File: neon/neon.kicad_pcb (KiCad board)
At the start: 2 copper layers, 60 x 50 mm, 45 parts, among them J2 V3V3-GND, J3 V3V3-GND, J4 V3V3-GND, J5 V3V3-VIO, Q1 BC807, Q2 BC807, Q3 BC807, Q4 BC807, Q5 BC807, Q6 BC807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

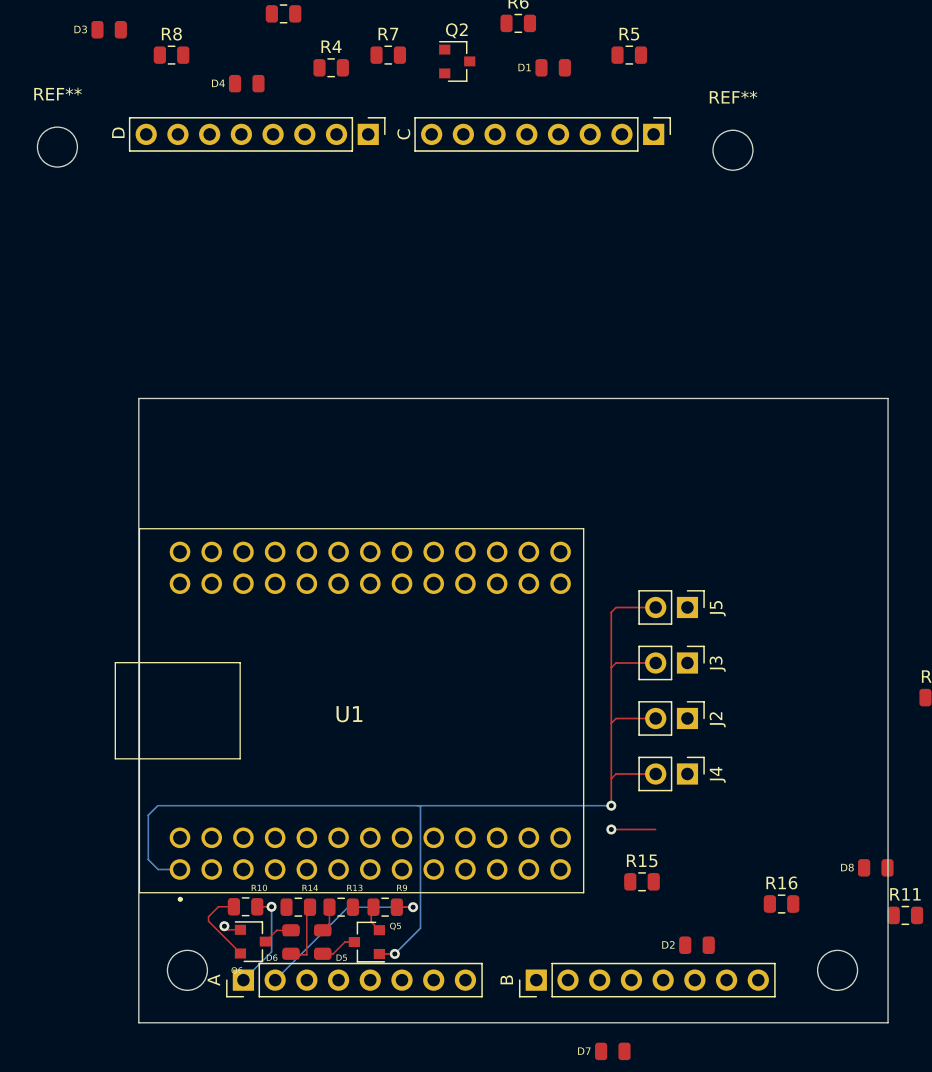
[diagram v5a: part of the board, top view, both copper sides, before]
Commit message: Labels adjustments
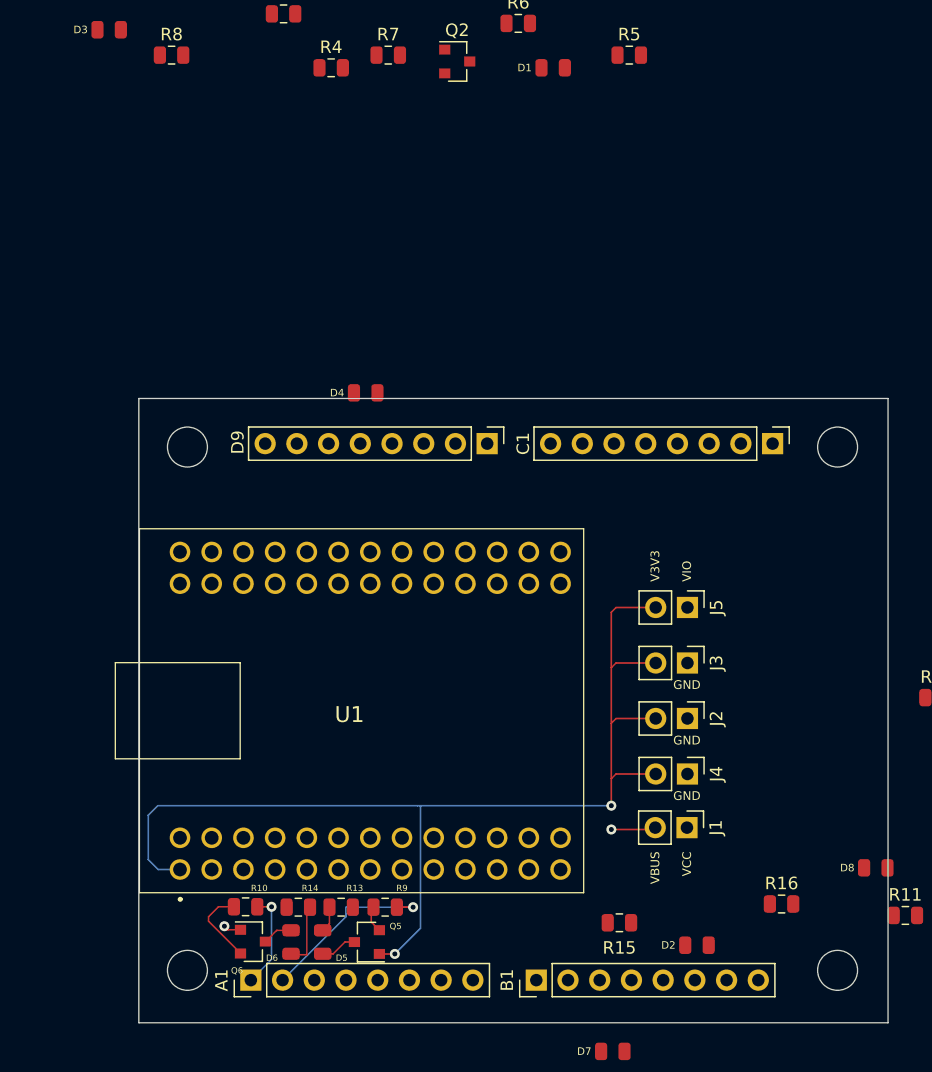
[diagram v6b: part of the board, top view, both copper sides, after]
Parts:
- removed the REF** at (163.1, 60.0)
- removed the REF** at (109.0, 59.8)
- added J1: VBUS-VCC, Connector_PinHeader_2.54mm:PinHeader_1x02_P2.54mm_Vertical, F.Cu at (159.4, 114.3)
- added REF**: MountingHole_3.2mm_M3, MountingHole:MountingHole_3.2mm_M3, F.Cu at (171.4, 83.8)
- added REF**: MountingHole_3.2mm_M3, MountingHole:MountingHole_3.2mm_M3, F.Cu at (119.4, 83.8)
- moved C1 26.5 mm to (166.2, 83.5)
- moved D4 26.5 mm to (133.7, 79.5)
- moved D9 26.5 mm to (143.4, 83.5)
- moved R15 3.75 mm to (154.0, 121.9)
- moved A1 0.60 mm to (124.5, 126.5)
- renumbered A to A1, B to B1, C to C1, D to D9
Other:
- board text added: "GND"
- board text added: "V3V3"
- board text added: "VBUS"
- board text added: "VCC"
- board text added: "VIO"
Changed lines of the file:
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@@
   (general
     (thickness 1.6)
-    (drawings 8)
-    (tracks 68)
+    (drawings 15)
+    (tracks 69)
     (zones 0)
-    (modules 45)
+    (modules 46)
     (nets 77)
   )
@@
     (add_net V3V3)
   )
+  (module Connector_PinHeader_2.54mm:PinHeader_1x02_P2.54mm_Vertical (layer F.Cu)
+    (at 159.385 114.3 270)
+    (descr "Through hole straight pin header, 1x02, 2.54mm pitch, single row")
+    (tags "Through hole pin header THT 1x02 2.54mm single row")
+    (fp_text reference J1 (at 0 -2.33 90) (layer F.SilkS)
+      (effects (font (size 1 1) (thickness 0.15)))
+    )
+    (fp_text value VBUS-VCC (at 0 4.87 90) (layer F.Fab)
+      (effects (font (size 1 1) (thickness 0.15)))
+    )
+    (fp_text user %R (at 0 1.27) (layer F.Fab)
+      (effects (font (size 1 1) (thickness 0.15)))
+    )
+    (fp_line (start -0.635 -1.27) (end 1.27 -1.27) (layer F.Fab) (width 0.1))
+    (fp_line (start 1.27 -1.27) (end 1.27 3.81) (layer F.Fab) (width 0.1))
+    (fp_line (start 1.27 3.81) (end -1.27 3.81) (layer F.Fab) (width 0.1))
+    (fp_line (start -1.27 3.81) (end -1.27 -0.635) (layer F.Fab) (width 0.1))
+    (fp_line (start -1.27 -0.635) (end -0.635 -1.27) (layer F.Fab) (width 0.1))
+    (fp_line (start -1.33 3.87) (end 1.33 3.87) (layer F.SilkS) (width 0.12))
+    (fp_line (start -1.33 1.27) (end -1.33 3.87) (layer F.SilkS) (width 0.12))
+    (fp_line (start 1.33 1.27) (end 1.33 3.87) (layer F.SilkS) (width 0.12))
+    (fp_line (start -1.33 1.27) (end 1.33 1.27) (layer F.SilkS) (width 0.12))
+    (fp_line (start -1.33 0) (end -1.33 -1.33) (layer F.SilkS) (width 0.12))
+    (fp_line (start -1.33 -1.33) (end 0 -1.33) (layer F.SilkS) (width 0.12))
+    (fp_line (start -1.8 -1.8) (end -1.8 4.35) (layer F.CrtYd) (width 0.05))
+    (fp_line (start -1.8 4.35) (end 1.8 4.35) (layer F.CrtYd) (width 0.05))
+    (fp_line (start 1.8 4.35) (end 1.8 -1.8) (layer F.CrtYd) (width 0.05))
+    (fp_line (start 1.8 -1.8) (end -1.8 -1.8) (layer F.CrtYd) (width 0.05))
+    (pad 2 thru_hole oval (at 0 2.54 270) (size 1.7 1.7) (drill 1) (layers *.Cu *.Mask)
+      (net 17 /FT4232H.sch/VBUS))
+    (pad 1 thru_hole rect (at 0 0 270) (size 1.7 1.7) (drill 1) (layers *.Cu *.Mask)
+      (net 50 /FT4232H.sch/VCC))
+    (model ${KISYS3DMOD}/Connector_PinHeader_2.54mm.3dshapes/PinHeader_1x02_P2.54mm_Vertical.wrl
+      (at (xyz 0 0 0))
+      (scale (xyz 1 1 1))
+      (rotate (xyz 0 0 0))
+    )
+  )
   (module Connector_PinHeader_2.54mm:PinHeader_1x08_P2.54mm_Vertical (layer F.Cu)
-    (at 123.8644 126.5136 90)
+    (at 124.46 126.5136 90)
     (descr "Through hole straight pin header, 1x08, 2.54mm pitch, single row")
     (tags "Through hole pin header THT 1x08 2.54mm single row")
-    (fp_text reference A (at 0 -2.33 90) (layer F.SilkS)
+    (fp_text reference A1 (at 0 -2.33 90) (layer F.SilkS)
       (effects (font (size 1 1) (thickness 0.15)))
     )
@@
   )
   (module neon_footprints:LED_0805_2012Metric (layer F.Cu)
-    (at 124.1295 54.716)
+    (at 133.6545 79.481)
     (descr "LED SMD 0805 (2012 Metric), square (rectangular) end terminal, IPC_7351 nominal, (Body size source: https://docs.google.com/spreadsheets/d/1BsfQQcO9C6DZCsRaXUlFlo91Tg2WpOkGARC1WS5S8t0/edit?usp=sharing), generated with kicad-footprint-generator")
     (tags diode)
@@
   )
   (module MountingHole:MountingHole_3.2mm_M3 (layer F.Cu)
-    (at 163.07 60.05)
+    (at 171.45 83.82)
     (descr "Mounting Hole 3.2mm, no annular, M3")
     (tags "mounting hole 3.2mm no annular m3")
     (attr virtual)
-    (fp_text reference REF** (at 0 -4.2) (layer F.SilkS)
+    (fp_text reference REF** (at 1.905 4.445) (layer F.SilkS) hide
       (effects (font (size 1 1) (thickness 0.15)))
     )
@@
   )
   (module MountingHole:MountingHole_3.2mm_M3 (layer F.Cu)
-    (at 108.968 59.796)
+    (at 119.38 83.82)
     (descr "Mounting Hole 3.2mm, no annular, M3")
     (tags "mounting hole 3.2mm no annular m3")
     (attr virtual)
-    (fp_text reference REF** (at 0 -4.2) (layer F.SilkS)
+    (fp_text reference REF** (at -1.27 4.445) (layer F.SilkS) hide
       (effects (font (size 1 1) (thickness 0.15)))
     )
@@
   )
   (module Resistor_SMD:R_0805_2012Metric (layer F.Cu)
-    (at 155.7899 118.6396)
+    (at 153.9725 121.92)
     (descr "Resistor SMD 0805 (2012 Metric), square (rectangular) end terminal, IPC_7351 nominal, (Body size source: https://docs.google.com/spreadsheets/d/1BsfQQcO9C6DZCsRaXUlFlo91Tg2WpOkGARC1WS5S8t0/edit?usp=sharing), generated with kicad-footprint-generator")
     (tags resistor)
     (attr smd)
-    (fp_text reference R15 (at 0 -1.65) (layer F.SilkS)
+    (fp_text reference R15 (at 0 2.0104) (layer F.SilkS)
       (effects (font (size 1 1) (thickness 0.15)))
     )
@@
   )
   (module Connector_PinHeader_2.54mm:PinHeader_1x08_P2.54mm_Vertical (layer F.Cu)
-    (at 156.72 58.78 270)
+    (at 166.245 83.545 270)
     (descr "Through hole straight pin header, 1x08, 2.54mm pitch, single row")
     (tags "Through hole pin header THT 1x08 2.54mm single row")
-    (fp_text reference C (at 0 19.974 90) (layer F.SilkS)
+    (fp_text reference C1 (at 0 19.974 90) (layer F.SilkS)
       (effects (font (size 1 1) (thickness 0.15)))
     )
@@
   )
   (module Connector_PinHeader_2.54mm:PinHeader_1x08_P2.54mm_Vertical (layer F.Cu)
-    (at 133.86 58.78 270)
+    (at 143.385 83.545 270)
     (descr "Through hole straight pin header, 1x08, 2.54mm pitch, single row")
     (tags "Through hole pin header THT 1x08 2.54mm single row")
-    (fp_text reference D (at -0.106 19.974 90) (layer F.SilkS)
+    (fp_text reference D9 (at -0.106 19.974 90) (layer F.SilkS)
       (effects (font (size 1 1) (thickness 0.15)))
     )
@@
     (descr "Through hole straight pin header, 1x08, 2.54mm pitch, single row")
     (tags "Through hole pin header THT 1x08 2.54mm single row")
-    (fp_text reference B (at 0 -2.33 90) (layer F.SilkS)
+    (fp_text reference B1 (at 0 -2.33 90) (layer F.SilkS)
       (effects (font (size 1 1) (thickness 0.15)))
     )
@@
       (rotate (xyz 0 0 0))
     )
+  )
+  (gr_text GND (at 159.385 111.76) (layer F.SilkS)
+    (effects (font (size 0.7 0.7) (thickness 0.175)))
+  )
+  (gr_text GND (at 159.385 107.315) (layer F.SilkS)
+    (effects (font (size 0.7 0.7) (thickness 0.175)))
+  )
+  (gr_text GND (at 159.385 102.87) (layer F.SilkS)
+    (effects (font (size 0.7 0.7) (thickness 0.175)))
+  )
+  (gr_text V3V3 (at 156.845 94.615 90) (layer F.SilkS)
+    (effects (font (size 0.7 0.7) (thickness 0.175)) (justify left))
+  )
+  (gr_text VIO (at 159.385 94.615 90) (layer F.SilkS)
+    (effects (font (size 0.7 0.7) (thickness 0.175)) (justify left))
+  )
+  (gr_text VBUS (at 156.845 116.205 90) (layer F.SilkS)
+    (effects (font (size 0.7 0.7) (thickness 0.175)) (justify right))
+  )
+  (gr_text VCC (at 159.385 116.205 90) (layer F.SilkS)
+    (effects (font (size 0.7 0.7) (thickness 0.175)) (justify right))
   )
   (dimension 3.84642 (width 0.15) (layer Dwgs.User)
@@
   (segment (start 137.3264 120.6716) (end 137.3264 120.6716) (width 0.127) (layer F.Cu) (net 32))
   (via (at 137.4534 120.6716) (size 0.8) (drill 0.4) (layers F.Cu B.Cu) (net 32))
-  (segment (start 132.2464 120.6716) (end 126.4044 126.5136) (width 0.127) (layer B.Cu) (net 32))
-  (segment (start 137.3264 120.6716) (end 132.2464 120.6716) (width 0.127) (layer B.Cu) (net 32))
+  (segment (start 127 126.5136) (end 132.08 121.4336) (width 0.127) (layer B.Cu) (net 32))
+  (segment (start 132.08 121.4336) (end 132.08 120.65) (width 0.127) (layer B.Cu) (net 32))
+  (segment (start 137.4534 120.6716) (end 132.1016 120.6716) (width 0.127) (layer B.Cu) (net 32))
   (via (at 126.1184 120.6396) (size 0.8) (drill 0.4) (layers F.Cu B.Cu) (net 33))
-  (segment (start 126.1184 124.2596) (end 123.8644 126.5136) (width 0.127) (layer B.Cu) (net 33))
-  (segment (start 126.1184 120.6396) (end 126.1184 124.2596) (width 0.127) (layer B.Cu) (net 33))
+  (segment (start 126.1184 124.8552) (end 124.46 126.5136) (width 0.127) (layer B.Cu) (net 33))
+  (segment (start 126.1184 120.6396) (end 126.1184 124.8552) (width 0.127) (layer B.Cu) (net 33))
 )

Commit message: Remove bak
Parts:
- moved B1 0.64 mm to (148.0, 126.5)
- moved A1 0.64 mm to (125.1, 126.5)
- moved C1 0.51 mm to (165.7, 83.5)
- moved D9 0.51 mm to (142.9, 83.5)
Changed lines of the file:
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@@
   )
   (module Connector_PinHeader_2.54mm:PinHeader_1x08_P2.54mm_Vertical (layer F.Cu)
-    (at 124.46 126.5136 90)
+    (at 125.095 126.5136 90)
     (descr "Through hole straight pin header, 1x08, 2.54mm pitch, single row")
     (tags "Through hole pin header THT 1x08 2.54mm single row")
@@
   )
   (module Connector_PinHeader_2.54mm:PinHeader_1x08_P2.54mm_Vertical (layer F.Cu)
-    (at 166.245 83.545 270)
+    (at 165.735 83.545 270)
     (descr "Through hole straight pin header, 1x08, 2.54mm pitch, single row")
     (tags "Through hole pin header THT 1x08 2.54mm single row")
@@
   )
   (module Connector_PinHeader_2.54mm:PinHeader_1x08_P2.54mm_Vertical (layer F.Cu)
-    (at 143.385 83.545 270)
+    (at 142.875 83.545 270)
     (descr "Through hole straight pin header, 1x08, 2.54mm pitch, single row")
     (tags "Through hole pin header THT 1x08 2.54mm single row")
@@
   )
   (module Connector_PinHeader_2.54mm:PinHeader_1x08_P2.54mm_Vertical (layer F.Cu)
-    (at 147.32 126.5136 90)
+    (at 147.955 126.5136 90)
     (descr "Through hole straight pin header, 1x08, 2.54mm pitch, single row")
     (tags "Through hole pin header THT 1x08 2.54mm single row")
@@
   (segment (start 137.3264 120.6716) (end 137.3264 120.6716) (width 0.127) (layer F.Cu) (net 32))
   (via (at 137.4534 120.6716) (size 0.8) (drill 0.4) (layers F.Cu B.Cu) (net 32))
-  (segment (start 127 126.5136) (end 132.08 121.4336) (width 0.127) (layer B.Cu) (net 32))
-  (segment (start 132.08 121.4336) (end 132.08 120.65) (width 0.127) (layer B.Cu) (net 32))
   (segment (start 137.4534 120.6716) (end 132.1016 120.6716) (width 0.127) (layer B.Cu) (net 32))
+  (segment (start 132.08 122.0686) (end 127.635 126.5136) (width 0.127) (layer B.Cu) (net 32))
+  (segment (start 132.08 120.65) (end 132.08 122.0686) (width 0.127) (layer B.Cu) (net 32))
   (via (at 126.1184 120.6396) (size 0.8) (drill 0.4) (layers F.Cu B.Cu) (net 33))
-  (segment (start 126.1184 124.8552) (end 124.46 126.5136) (width 0.127) (layer B.Cu) (net 33))
-  (segment (start 126.1184 120.6396) (end 126.1184 124.8552) (width 0.127) (layer B.Cu) (net 33))
+  (segment (start 126.1184 125.4902) (end 125.095 126.5136) (width 0.127) (layer B.Cu) (net 33))
+  (segment (start 126.1184 120.6396) (end 126.1184 125.4902) (width 0.127) (layer B.Cu) (net 33))
 )

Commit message: With transistors
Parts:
- U2: renamed from A1; value ABUS -> A
- U3: renamed from B1; value BBUS -> B
- U4: renamed from C1; value CBUS -> C
- U5: renamed from D9; value DBUS -> D
- moved J5 21.7 mm to (170.8, 95.9)
- moved J1 20.6 mm to (170.9, 113.8)
- moved J2 11.4 mm to (170.9, 109.4)
- moved J3 11.4 mm to (170.9, 104.9)
- moved J4 11.4 mm to (170.9, 100.5)
- moved D4 8.25 mm to (134.9, 87.6)
- renumbered J5 to J1, J4 to J2, J2 to J3, J3 to J4, J1 to J5
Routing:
- net /FT4232H.sch/VBUS: track 3.61 -> 43.5 mm, vias 1 -> 0
- net V3V3: track 89.6 -> 100.2 mm, vias 3 -> 4
- net /FT4232H.sch/VIO: track 0.00 -> 4.74 mm
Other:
- board text added: "3V3"
- board text removed: "V3V3"
